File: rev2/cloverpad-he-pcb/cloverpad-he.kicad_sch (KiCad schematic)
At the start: 51 parts, among them J1 USB_C_Receptacle_USB2.0, SW1 SW_Push, SW2 SW_Push, U1 SRV05-4, U2 XC6206P332MR, U3 DRV5056AxxDBZxQ1, U4 DRV5056AxxDBZxQ1, U5 DRV5056AxxDBZxQ1, U8 RP2040, U9 W25Q16JVSSIQ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

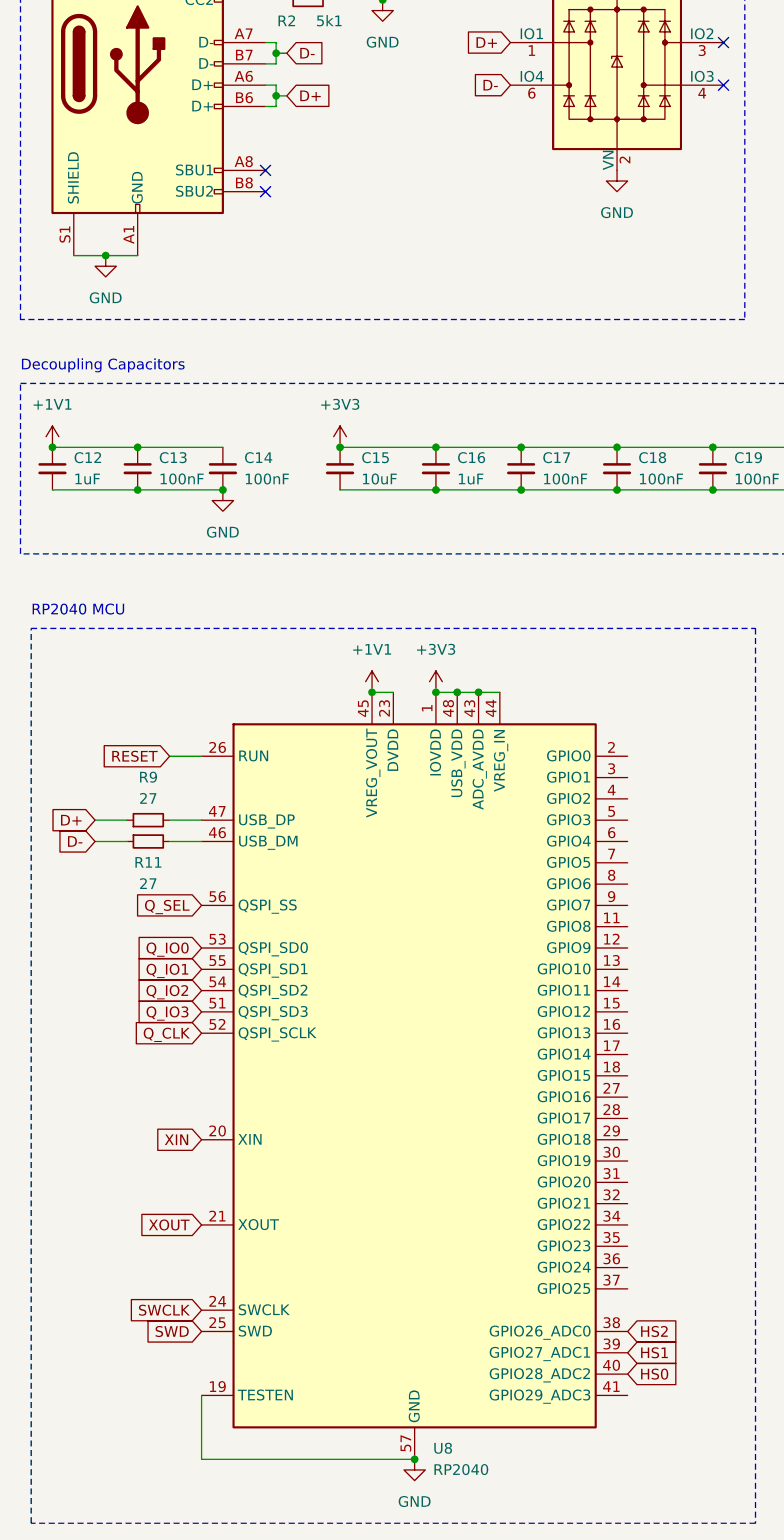
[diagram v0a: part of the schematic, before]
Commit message: chore: update all symbols + footprints to match kicad 8
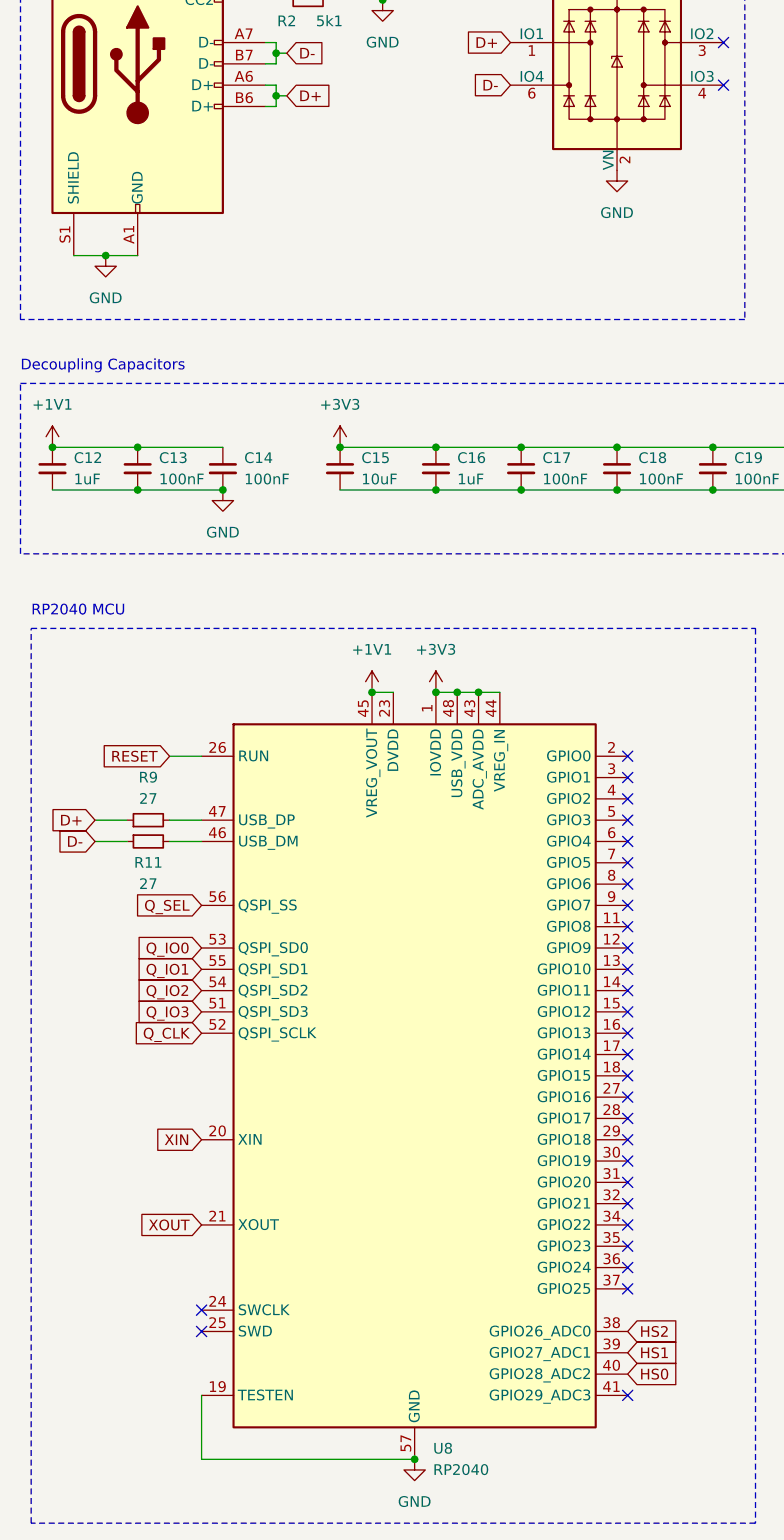
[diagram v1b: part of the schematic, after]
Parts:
- J1: symbol Connector:USB_C_Receptacle_USB2.0 -> Connector:USB_C_Receptacle_USB2.0_14P
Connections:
- net SWCLK: no longer names the net of U8.24 (SWCLK)
- net SWD: no longer names the net of U8.25 (SWD)
- no-connect marks 4 -> 31

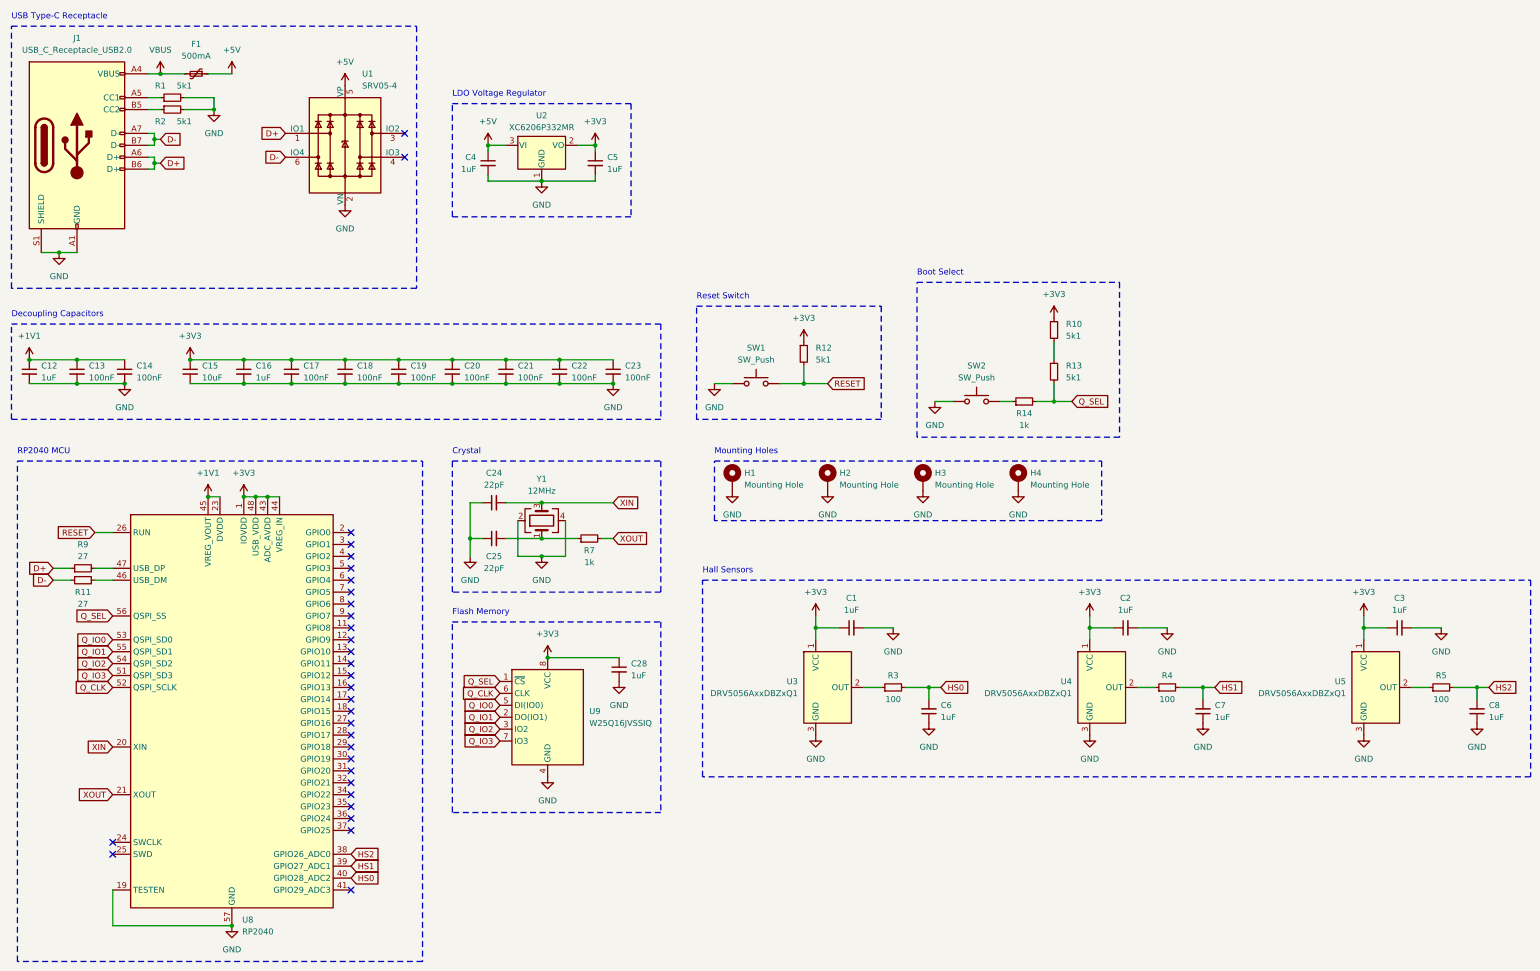
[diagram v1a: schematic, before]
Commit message: feat(r2): initial attempt at shrinking case + pcb
Case: 75x65mm, PCB: 60x50mm (57.5mm height including USB-C cutout)

I'm able to get ~3mm wall thickness around the threaded inserts, which gives me a bit more confidence in the walls not cracking.
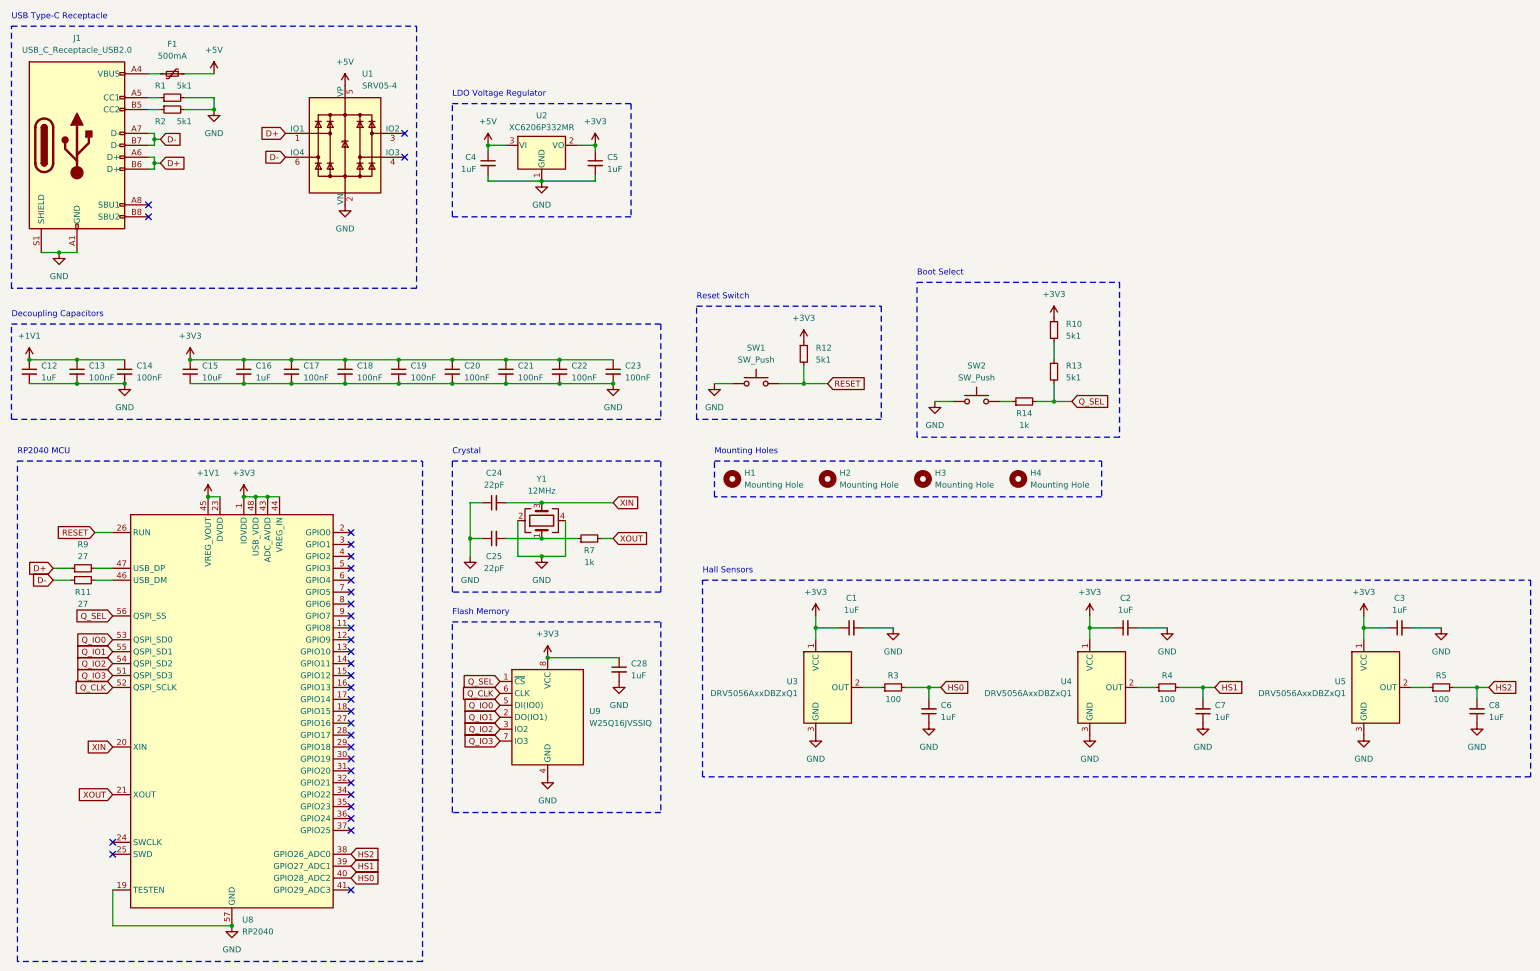
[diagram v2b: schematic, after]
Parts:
- H1, H2, H3, H4: footprint MountingHole:MountingHole_2.2mm_M2_Pad -> MountingHole:MountingHole_2.2mm_M2; symbol Mechanical:MountingHole_Pad -> Mechanical:MountingHole; now in the parts list
- J1: symbol Connector:USB_C_Receptacle_USB2.0_14P -> Connector:USB_C_Receptacle_USB2.0_16P
- U3, U4, U5: footprint Package_TO_SOT_SMD:SOT-23 -> Custom:KS-20-1U-DRV5056
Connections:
- net GND: no longer H1.1, H2.1, H3.1, H4.1
- net VBUS: no longer names the net of F1.2, J1.A4 (VBUS), J1.A9 (VBUS), J1.B4 (VBUS), J1.B9 (VBUS)
- no-connect marks 31 -> 33
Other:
- moved on the sheet: F1
